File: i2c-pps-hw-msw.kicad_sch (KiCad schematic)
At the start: 13 parts, among them J1 +5V, Q5 SIS413DN, Q6 MMBT3904, Q8 SIS413DN

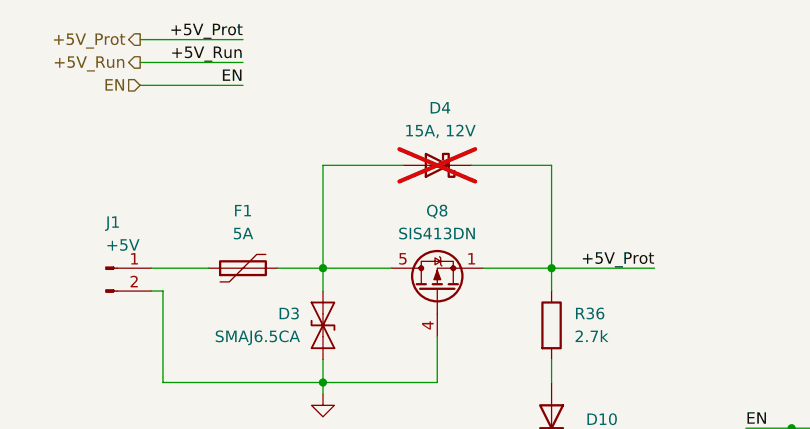
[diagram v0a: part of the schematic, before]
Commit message: Setup the board and move components from schematics
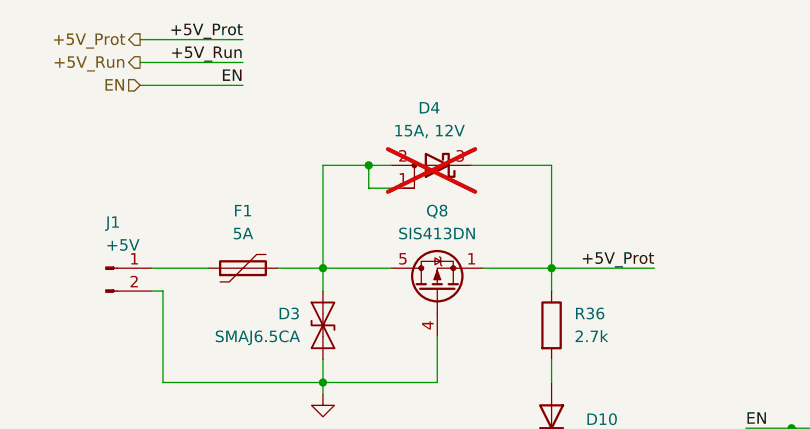
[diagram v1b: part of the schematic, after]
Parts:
- D4: symbol Device:D_Schottky -> Device:D_Schottky_AAK
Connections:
- net +5V_Prot: now also D4.3 (K); no longer D4.1 (K)
- net at D3.2 (A2), D4.2 (A), F1.2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: now also D4.1 (A)
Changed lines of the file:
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@@
+	)
+	(junction
+		(at 110.49 90.17)
+		(diameter 0)
+		(color 0 0 0 0)
 	)
 	(junction
@@
 	(wire
 		(pts
+			(xy 110.49 90.17) (xy 113.03 90.17)
+		)
+		(stroke
+			(width 0)
+			(type default)
+		)
+	)
+	(wire
+		(pts
 			(xy 105.41 114.3) (xy 87.63 114.3)
 		)
@@
 	(wire
 		(pts
+			(xy 113.03 92.71) (xy 110.49 92.71)
+		)
+		(stroke
+			(width 0)
+			(type default)
+		)
+	)
+	(wire
+		(pts
 			(xy 118.11 109.22) (xy 118.11 114.3)
 		)
@@
 	(wire
 		(pts
+			(xy 110.49 92.71) (xy 110.49 90.17)
+		)
+		(stroke
+			(width 0)
+			(type default)
+		)
+	)
+	(wire
+		(pts
 			(xy 130.81 101.6) (xy 142.24 101.6)
 		)
@@
 	(wire
 		(pts
-			(xy 105.41 90.17) (xy 114.3 90.17)
+			(xy 105.41 90.17) (xy 110.49 90.17)
 		)
 		(stroke
@@
 	)
 	(symbol
-		(lib_id "Device:D_Schottky")
+		(lib_id "Device:D_Schottky_AAK")
 		(at 118.11 90.17 180)
 		(unit 1)
@@
 		(fields_autoplaced yes)
 		(property "Reference" "D4"
-			(at 118.4275 83.82 0)
+			(at 117.221 83.82 0)
 			(effects
 				(font
@@
 		)
 		(property "Value" "15A, 12V"
-			(at 118.4275 86.36 0)
+			(at 117.221 86.36 0)
 			(effects
 				(font
@@
 			)
 		)
-		(property "Datasheet" "https://www.onsemi.com/pdf/datasheet/fsv15100v-d.pdf"
+		(property "Datasheet" "~"
 			(at 118.11 90.17 0)
 			(effects
@@
 			)
 		)
-		(property "Description" "< 0.7V"
+		(property "Description" "Schottky diode, anode on pins 1 and 2"
 			(at 118.11 90.17 0)
 			(effects
@@
 		(pin "1"
 		)
+		(pin "3"
+		)
 		(instances

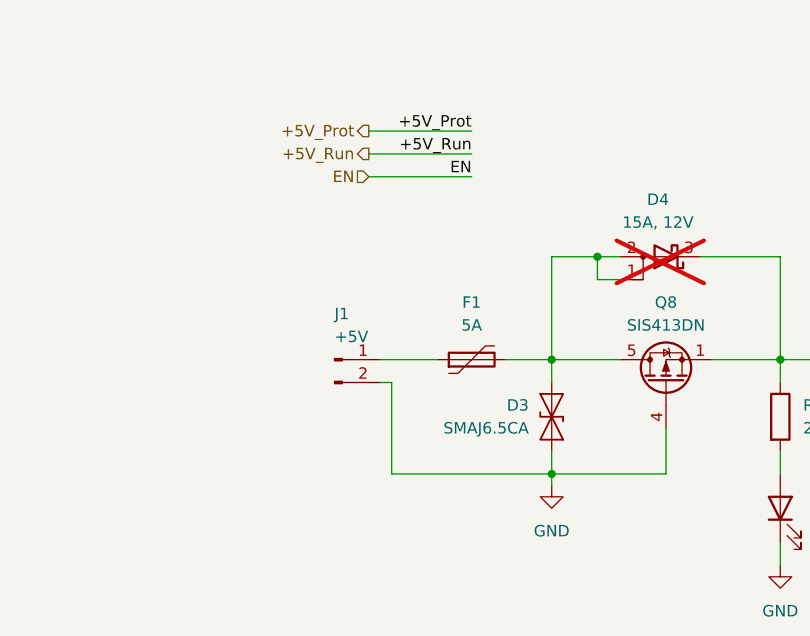
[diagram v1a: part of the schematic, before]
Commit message: Implement approximate component placement
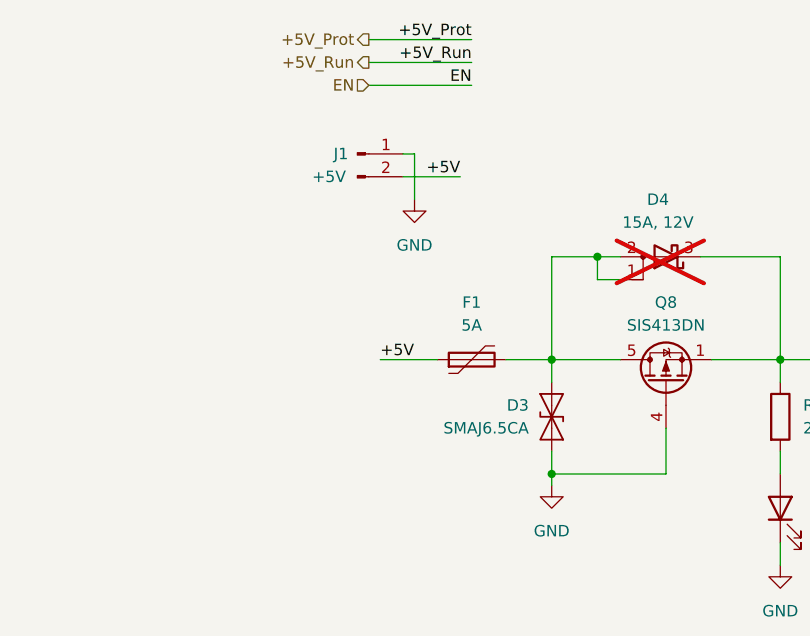
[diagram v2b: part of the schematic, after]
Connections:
- net GND: now also J1.1 (Pin_1); no longer J1.2 (Pin_2)
- net +5V: now reaches F1.1
- net +5V: now also J1.2 (Pin_2); no longer J1.1 (Pin_1)
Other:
- moved on the sheet: J1
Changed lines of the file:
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@@
+	(wire
+		(pts
+			(xy 90.17 78.74) (xy 90.17 83.82)
+		)
+		(stroke
+			(width 0)
+			(type default)
+		)
+	)
 	(wire
 		(pts
@@
 	(wire
 		(pts
-			(xy 85.09 76.2) (xy 96.52 76.2)
+			(xy 85.09 66.04) (xy 96.52 66.04)
+		)
+		(stroke
+			(width 0)
+			(type default)
+		)
+	)
+	(wire
+		(pts
+			(xy 95.25 81.28) (xy 88.9 81.28)
 		)
 		(stroke
@@
 	(wire
 		(pts
-			(xy 85.09 78.74) (xy 96.52 78.74)
+			(xy 85.09 68.58) (xy 96.52 68.58)
 		)
 		(stroke
@@
 	(wire
 		(pts
-			(xy 105.41 114.3) (xy 87.63 114.3)
-		)
-		(stroke
-			(width 0)
-			(type default)
-		)
-	)
-	(wire
-		(pts
 			(xy 130.81 121.92) (xy 130.81 124.46)
 		)
@@
 	(wire
 		(pts
+			(xy 86.36 101.6) (xy 92.71 101.6)
+		)
+		(stroke
+			(width 0)
+			(type default)
+		)
+	)
+	(wire
+		(pts
 			(xy 123.19 101.6) (xy 130.81 101.6)
 		)
@@
 	(wire
 		(pts
-			(xy 85.09 81.28) (xy 96.52 81.28)
+			(xy 85.09 71.12) (xy 96.52 71.12)
 		)
 		(stroke
@@
 	(wire
 		(pts
-			(xy 87.63 104.14) (xy 87.63 114.3)
-		)
-		(stroke
-			(width 0)
-			(type default)
-		)
-	)
-	(wire
-		(pts
-			(xy 86.36 101.6) (xy 92.71 101.6)
-		)
-		(stroke
-			(width 0)
-			(type default)
-		)
-	)
-	(wire
-		(pts
 			(xy 157.48 139.7) (xy 157.48 142.24)
 		)
@@
 	(wire
 		(pts
+			(xy 88.9 78.74) (xy 90.17 78.74)
+		)
+		(stroke
+			(width 0)
+			(type default)
+		)
+	)
+	(wire
+		(pts
 			(xy 105.41 90.17) (xy 105.41 101.6)
-		)
-		(stroke
-			(width 0)
-			(type default)
-		)
-	)
-	(wire
-		(pts
-			(xy 86.36 104.14) (xy 87.63 104.14)
 		)
 		(stroke
@@
 	)
 	(label "+5V_Prot"
-		(at 96.52 76.2 180)
+		(at 96.52 66.04 180)
 		(effects
 			(font
@@
 		)
 	)
-	(label "+5V_Run"
-		(at 96.52 78.74 180)
+	(label "+5V"
+		(at 95.25 81.28 180)
 		(effects
 			(font
@@
 		)
 	)
-	(label "EN"
-		(at 96.52 81.28 180)
+	(label "+5V_Run"
+		(at 96.52 68.58 180)
 		(effects
 			(font
@@
 		)
 	)
-	(hierarchical_label "+5V_Run"
-		(shape output)
-		(at 85.09 78.74 180)
+	(label "EN"
+		(at 96.52 71.12 180)
 		(effects
 			(font
 				(size 1.27 1.27)
 			)
-			(justify right)
-		)
-	)
-	(hierarchical_label "+5V_Prot"
-		(shape output)
-		(at 85.09 76.2 180)
+			(justify right bottom)
+		)
+	)
+	(label "+5V"
+		(at 86.36 101.6 0)
 		(effects
 			(font
 				(size 1.27 1.27)
 			)
-			(justify right)
-		)
-	)
-	(hierarchical_label "EN"
-		(shape input)
-		(at 85.09 81.28 180)
+			(justify left bottom)
+		)
+	)
+	(hierarchical_label "+5V_Run"
+		(shape output)
+		(at 85.09 68.58 180)
 		(effects
 			(font
@@
 		)
 	)
+	(hierarchical_label "+5V_Prot"
+		(shape output)
+		(at 85.09 66.04 180)
+		(effects
+			(font
+				(size 1.27 1.27)
+			)
+			(justify right)
+		)
+	)
+	(hierarchical_label "EN"
+		(shape input)
+		(at 85.09 71.12 180)
+		(effects
+			(font
+				(size 1.27 1.27)
+			)
+			(justify right)
+		)
+	)
 	(symbol
 		(lib_id "Connector:Conn_01x02_Pin")
-		(at 81.28 101.6 0)
+		(at 83.82 78.74 0)
 		(unit 1)
 		(exclude_from_sim no)
@@
 		(dnp no)
 		(property "Reference" "J1"
-			(at 81.28 96.52 0)
-			(effects
-				(font
-					(size 1.27 1.27)
-				)
-				(justify left)
+			(at 82.804 78.74 0)
+			(effects
+				(font
+					(size 1.27 1.27)
+				)
+				(justify right)
 			)
 		)
 		(property "Value" "+5V"
-			(at 81.28 99.06 0)
-			(effects
-				(font
-					(size 1.27 1.27)
-				)
-				(justify left)
+			(at 82.55 81.28 0)
+			(effects
+				(font
+					(size 1.27 1.27)
+				)
+				(justify right)
 			)
 		)
 		(property "Footprint" "i2c-pps-hw:TE_1-1123724-2"
-			(at 81.28 101.6 0)
+			(at 83.82 78.74 0)
 			(effects
 				(font
@@
 		)
 		(property "Datasheet" "https://www.te.com/commerce/DocumentDelivery/DDEController?Action=srchrtrv&DocNm=411-5899&DocType=SS&DocLang=Japanese"
-			(at 81.28 101.6 0)
+			(at 83.82 78.74 0)
 			(effects
 				(font
@@
 		)
 		(property "Description" "Header, 3(2) position"
-			(at 81.28 101.6 0)
+			(at 83.82 78.74 0)
 			(effects
 				(font
@@
 		)
 		(property "Manufacturer" "TE Connectivity AMP Connectors"
-			(at 81.28 101.6 0)
+			(at 83.82 78.74 0)
 			(effects
 				(font
@@
 		)
 		(property "Part Number" "1-1123724-2"
-			(at 81.28 101.6 0)
+			(at 83.82 78.74 0)
 			(effects
 				(font
@@
 					(unit 1)
 				)
+			)
+		)
+	)
+	(symbol
+		(lib_id "power:GND")
+		(at 90.17 83.82 0)
+		(unit 1)
+		(exclude_from_sim no)
+		(in_bom yes)
+		(on_board yes)
+		(dnp no)
+		(fields_autoplaced yes)
+		(property "Reference" "#PWR041"
+			(at 90.17 90.17 0)
+			(effects
+				(font
+					(size 1.27 1.27)
+				)
+				(hide yes)
+			)
+		)
+		(property "Value" "GND"
+			(at 90.17 88.9 0)
+			(effects
+				(font
+					(size 1.27 1.27)
+				)
+			)
+		)
+		(property "Footprint" ""
+			(at 90.17 83.82 0)
+			(effects
+				(font
+					(size 1.27 1.27)
+				)
+				(hide yes)
+			)
+		)
+		(property "Datasheet" ""
+			(at 90.17 83.82 0)
+			(effects
+				(font
+					(size 1.27 1.27)
+				)
+				(hide yes)
+			)
+		)
+		(property "Description" "Power symbol creates a global label with name \"GND\" , ground"
+			(at 90.17 83.82 0)
+			(effects
+				(font
+					(size 1.27 1.27)
+				)
+				(hide yes)
+			)
+		)
+		(pin "1"
+		)
+		(instances
+			(project "i2c-pps-hw"
+				(path "/512c4d3f-92f6-4670-bf9b-2123d46bbde3/242a0190-1834-4b2f-bfa7-cf55bc2f9217"
+					(reference "#PWR041")
+					(unit 1)
+				)

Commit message: Add thermal vias to the master switch components
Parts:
- D4: footprint Package_TO_SOT_SMD:TO-277A -> i2c-pps-hw:TO-277A_ThermalVias
- Q5, Q8: footprint Package_SO:Vishay_PowerPAK_1212-8_Single -> i2c-pps-hw:Vishay_PowerPAK_1212-8_Single_ThermalVias
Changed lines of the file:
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@@
 			)
 		)
-		(property "Footprint" "Package_TO_SOT_SMD:TO-277A"
+		(property "Footprint" "i2c-pps-hw:TO-277A_ThermalVias"
 			(at 118.11 90.17 0)
 			(effects
@@
 			)
 		)
-		(property "Footprint" "Package_SO:Vishay_PowerPAK_1212-8_Single"
+		(property "Footprint" "i2c-pps-hw:Vishay_PowerPAK_1212-8_Single_ThermalVias"
 			(at 120.015 99.06 0)
 			(effects
@@
 			)
 		)
-		(property "Footprint" "Package_SO:Vishay_PowerPAK_1212-8_Single"
+		(property "Footprint" "i2c-pps-hw:Vishay_PowerPAK_1212-8_Single_ThermalVias"
 			(at 188.595 99.06 0)
 			(effects
